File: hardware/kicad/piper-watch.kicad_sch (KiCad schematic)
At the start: 0 parts

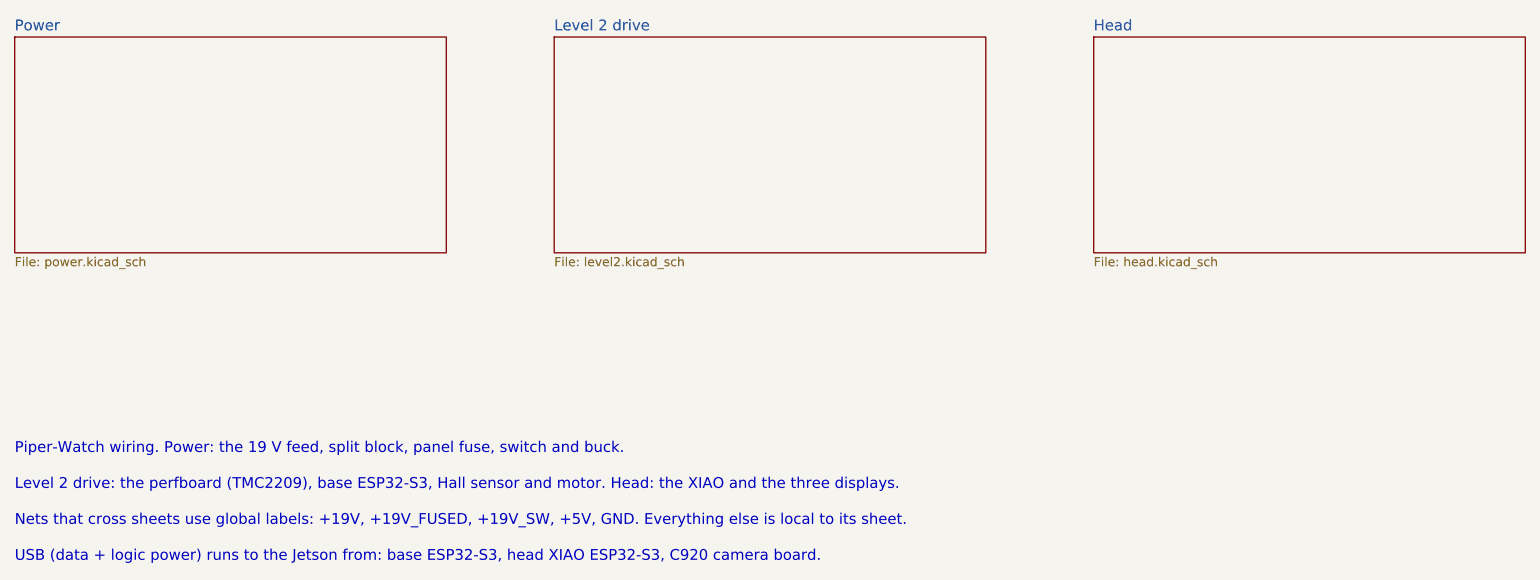
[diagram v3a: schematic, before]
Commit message: One ESP32: the JC4827W543R display's ESP32-S3 runs the pan motor - J4 lead from its P3 (IO15 STEP, IO16 DIR, IO6 EN, IO7 HALL) and P4 (3.3V, GND); R2 now fitted; base DevKit dropped from wiring.md, schematic, READMEs
Co-Authored-By: Claude Opus 5.5 <noreply@anthropic.com>
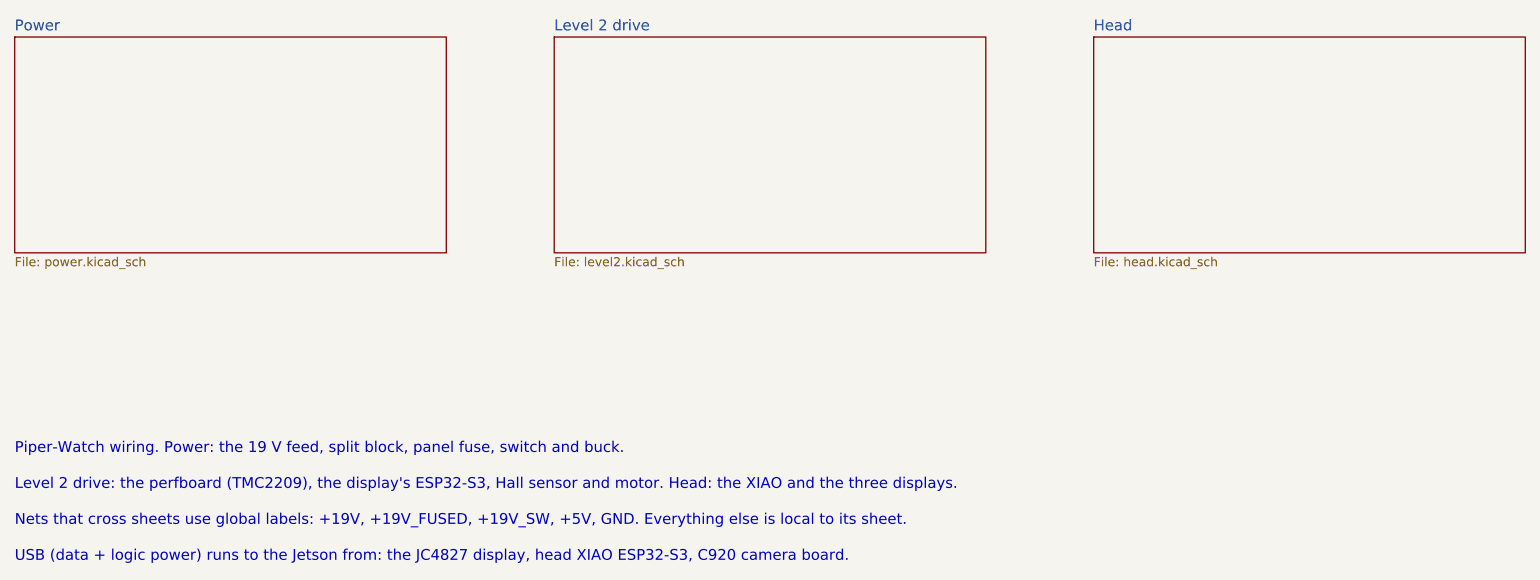
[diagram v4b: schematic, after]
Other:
- note added: "Level 2 drive: the perfboard (TMC2209), the display's ESP32-S3, Hall sensor and motor. Head: the XIAO and the three displays."
- note added: "USB (data + logic power) runs to the Jetson from: the JC4827 display, head XIAO ESP32-S3, C920 camera board."
- note removed: "Level 2 drive: the perfboard (TMC2209), base ESP32-S3, Hall sensor and motor. Head: the XIAO and the three displays."
- note removed: "USB (data + logic power) runs to the Jetson from: base ESP32-S3, head XIAO ESP32-S3, C920 camera board."
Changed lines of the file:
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@@
 (sheet (at 182.88 60.96) (size 60.96 30.48) (exclude_from_sim no) (in_bom yes) (on_board yes) (dnp no) (stroke (width 0.1524) (type solid)) (fill (color 0 0 0 0.0000)) (property "Sheetname" "Head" (at 182.88 60.2 0) (effects (font (size 1.524 1.524)) (justify left bottom))) (property "Sheetfile" "head.kicad_sch" (at 182.88 92.0 0) (effects (font (size 1.27 1.27)) (justify left top))) (instances (project "piper-watch" (path "/833d4739-1417-5dca-9991-7683c6f341a1" (page "4")))))
 (text "Piper-Watch wiring. Power: the 19 V feed, split block, panel fuse, switch and buck." (exclude_from_sim no) (at 30.48 120 0) (effects (font (size 1.524 1.524)) (justify left bottom)))
-(text "Level 2 drive: the perfboard (TMC2209), base ESP32-S3, Hall sensor and motor. Head: the XIAO and the three displays." (exclude_from_sim no) (at 30.48 125.08 0) (effects (font (size 1.524 1.524)) (justify left bottom)))
+(text "Level 2 drive: the perfboard (TMC2209), the display's ESP32-S3, Hall sensor and motor. Head: the XIAO and the three displays." (exclude_from_sim no) (at 30.48 125.08 0) (effects (font (size 1.524 1.524)) (justify left bottom)))
 (text "Nets that cross sheets use global labels: +19V, +19V_FUSED, +19V_SW, +5V, GND. Everything else is local to its sheet." (exclude_from_sim no) (at 30.48 130.16 0) (effects (font (size 1.524 1.524)) (justify left bottom)))
-(text "USB (data + logic power) runs to the Jetson from: base ESP32-S3, head XIAO ESP32-S3, C920 camera board." (exclude_from_sim no) (at 30.48 135.24 0) (effects (font (size 1.524 1.524)) (justify left bottom)))
+(text "USB (data + logic power) runs to the Jetson from: the JC4827 display, head XIAO ESP32-S3, C920 camera board." (exclude_from_sim no) (at 30.48 135.24 0) (effects (font (size 1.524 1.524)) (justify left bottom)))
 (sheet_instances (path "/" (page "1")))
 (embedded_fonts no))
